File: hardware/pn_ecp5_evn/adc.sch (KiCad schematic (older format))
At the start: 33 parts, among them U801 THS4551, U802 LT6657BHMS8-2.5

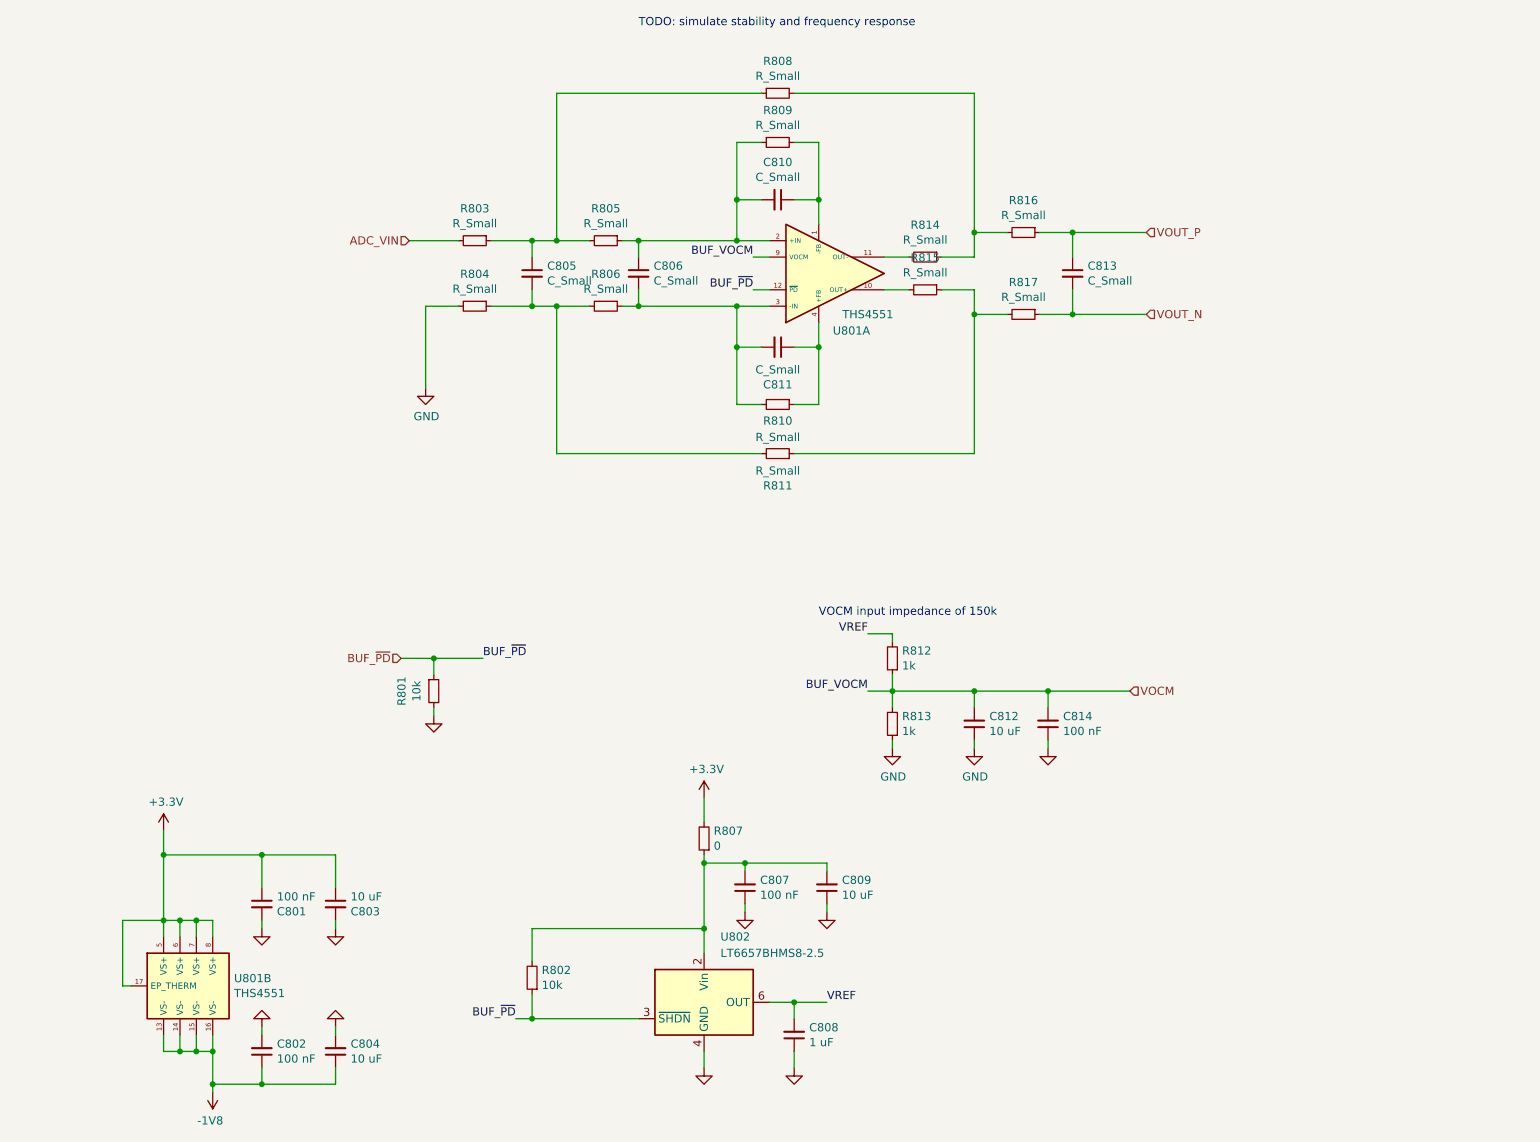
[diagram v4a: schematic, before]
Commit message: checked stability of LO amplifier, started migen project, added more flexibility for active filtering on baseband path
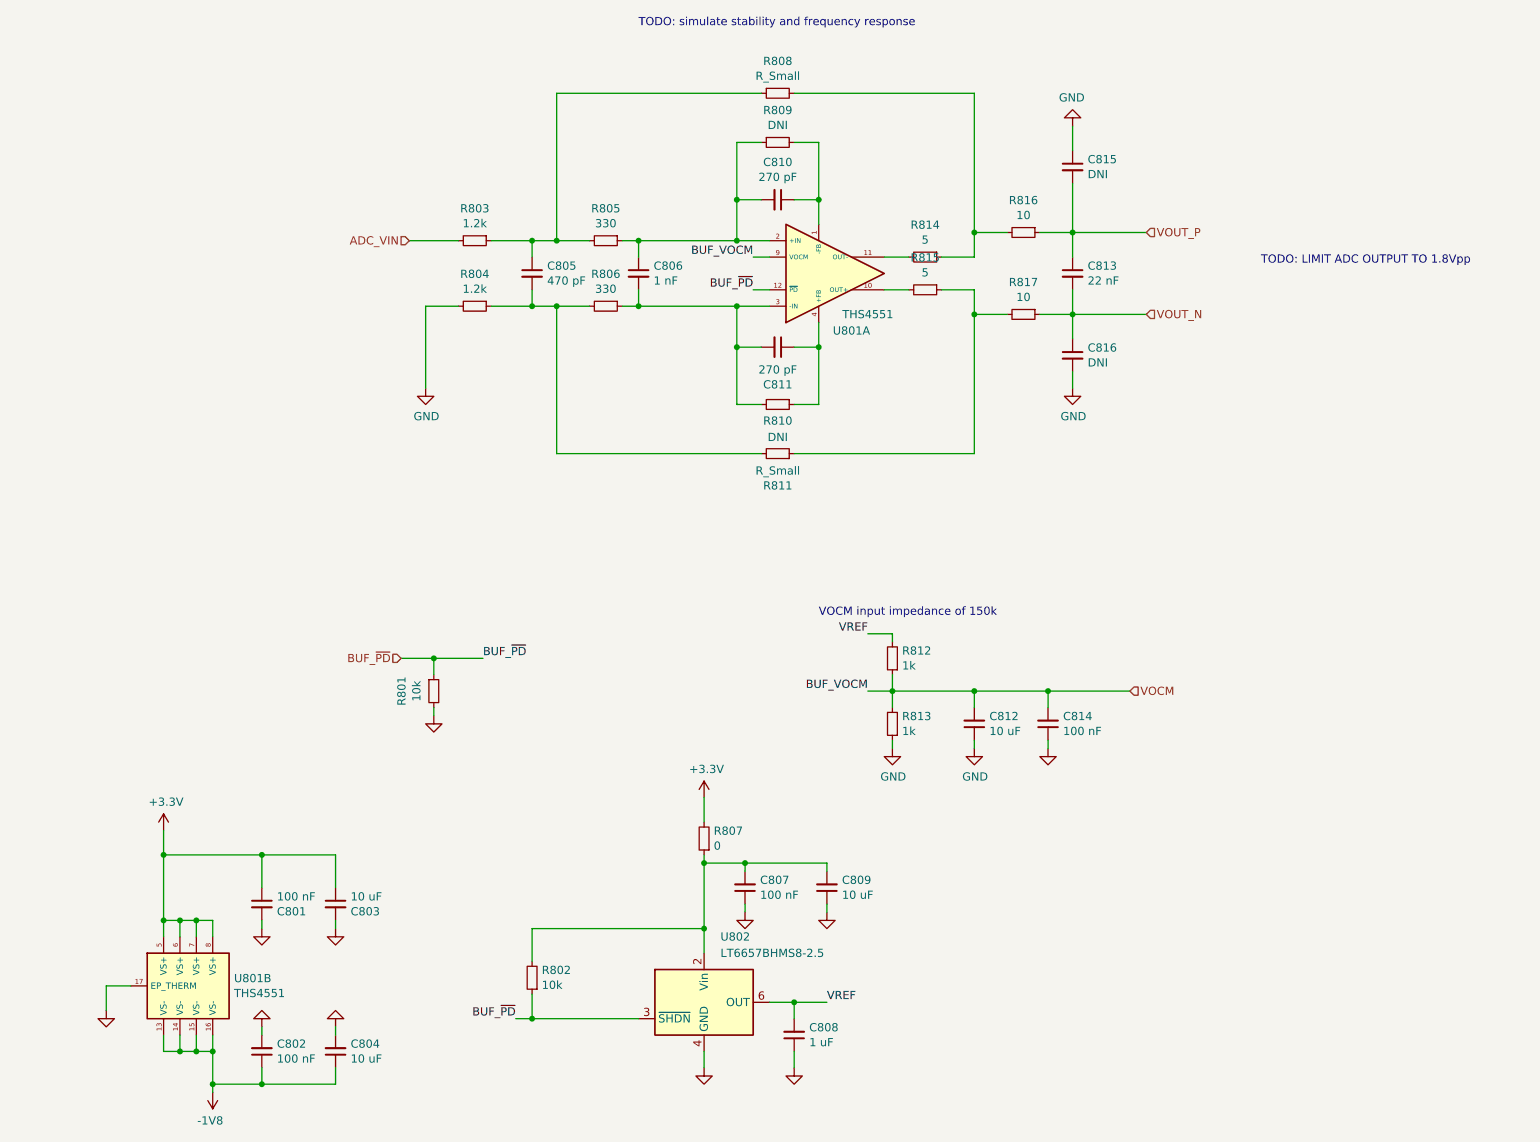
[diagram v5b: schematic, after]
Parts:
- added C815, C816: DNI, Capacitor_SMD:C_0402_1005Metric, symbol Device:C_Small
- C805: value C_Small -> 470 pF; footprint Capacitor_SMD:C_0402_1005Metric -> Capacitor_SMD:C_0603_1608Metric
- C806: value C_Small -> 1 nF
- C810, C811: value C_Small -> 270 pF; footprint Capacitor_SMD:C_0402_1005Metric -> Capacitor_SMD:C_0603_1608Metric
- C813: value C_Small -> 22 nF
- R803, R804: value R_Small -> 1.2k
- R805, R806: value R_Small -> 330
- R809, R810: value R_Small -> DNI
- R814, R815: value R_Small -> 5
- R816, R817: value R_Small -> 10
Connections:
- net +3V3: no longer U801.17 (EP_THERM)
- net GND: now also U801.17 (EP_THERM), C815.1, C816.2
- net VOUT_N: now also C816.1
- net VOUT_P: now also C815.2
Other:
- note added: "TODO: LIMIT ADC OUTPUT TO 1.8Vpp"
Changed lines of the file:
@@
 	2450 6250 2450 6200
-Wire Wire Line
-	1200 6600 1150 6600
-Wire Wire Line
-	1150 6600 1150 6200
-Wire Wire Line
-	1150 6200 1400 6200
 Wire Wire Line
 	2000 5800 2000 6000
@@
 P 6050 2150
 F 0 "R814" V 5854 2150 50  0000 C CNN
-F 1 "R_Small" V 5945 2150 50  0000 C CNN
+F 1 "5" V 5945 2150 50  0000 C CNN
 F 2 "Resistor_SMD:R_0402_1005Metric" H 6050 2150 50  0001 C CNN
 F 3 "~" H 6050 2150 50  0001 C CNN
@@
 P 6050 2350
 F 0 "R815" V 5854 2350 50  0000 C CNN
-F 1 "R_Small" V 5945 2350 50  0000 C CNN
+F 1 "5" V 5945 2350 50  0000 C CNN
 F 2 "Resistor_SMD:R_0402_1005Metric" H 6050 2350 50  0001 C CNN
 F 3 "~" H 6050 2350 50  0001 C CNN
@@
 P 4100 2050
 F 0 "R805" V 3904 2050 50  0000 C CNN
-F 1 "R_Small" V 3995 2050 50  0000 C CNN
+F 1 "330" V 3995 2050 50  0000 C CNN
 F 2 "Resistor_SMD:R_0402_1005Metric" H 4100 2050 50  0001 C CNN
 F 3 "~" H 4100 2050 50  0001 C CNN
@@
 P 4300 2250
 F 0 "C806" H 4392 2296 50  0000 L CNN
-F 1 "C_Small" H 4392 2205 50  0000 L CNN
+F 1 "1 nF" H 4392 2205 50  0000 L CNN
 F 2 "Capacitor_SMD:C_0402_1005Metric" H 4300 2250 50  0001 C CNN
 F 3 "~" H 4300 2250 50  0001 C CNN
@@
 P 5150 2700
 F 0 "C811" V 4921 2700 50  0000 C CNN
-F 1 "C_Small" V 5012 2700 50  0000 C CNN
-F 2 "Capacitor_SMD:C_0402_1005Metric" H 5150 2700 50  0001 C CNN
+F 1 "270 pF" V 5012 2700 50  0000 C CNN
+F 2 "Capacitor_SMD:C_0603_1608Metric" H 5150 2700 50  0001 C CNN
 F 3 "~" H 5150 2700 50  0001 C CNN
 	1    5150 2700
@@
 P 4100 2450
 F 0 "R806" V 3904 2450 50  0000 C CNN
-F 1 "R_Small" V 3995 2450 50  0000 C CNN
+F 1 "330" V 3995 2450 50  0000 C CNN
 F 2 "Resistor_SMD:R_0402_1005Metric" H 4100 2450 50  0001 C CNN
 F 3 "~" H 4100 2450 50  0001 C CNN
@@
 P 3650 2250
 F 0 "C805" H 3742 2296 50  0000 L CNN
-F 1 "C_Small" H 3742 2205 50  0000 L CNN
-F 2 "Capacitor_SMD:C_0402_1005Metric" H 3650 2250 50  0001 C CNN
+F 1 "470 pF" H 3742 2205 50  0000 L CNN
+F 2 "Capacitor_SMD:C_0603_1608Metric" H 3650 2250 50  0001 C CNN
 F 3 "~" H 3650 2250 50  0001 C CNN
 	1    3650 2250
@@
 P 5150 1800
 F 0 "C810" V 4921 1800 50  0000 C CNN
-F 1 "C_Small" V 5012 1800 50  0000 C CNN
-F 2 "Capacitor_SMD:C_0402_1005Metric" H 5150 1800 50  0001 C CNN
+F 1 "270 pF" V 5012 1800 50  0000 C CNN
+F 2 "Capacitor_SMD:C_0603_1608Metric" H 5150 1800 50  0001 C CNN
 F 3 "~" H 5150 1800 50  0001 C CNN
 	1    5150 1800
@@
 P 3300 2450
 F 0 "R804" V 3104 2450 50  0000 C CNN
-F 1 "R_Small" V 3195 2450 50  0000 C CNN
+F 1 "1.2k" V 3195 2450 50  0000 C CNN
 F 2 "Resistor_SMD:R_0402_1005Metric" H 3300 2450 50  0001 C CNN
 F 3 "~" H 3300 2450 50  0001 C CNN
@@
 P 3300 2050
 F 0 "R803" V 3104 2050 50  0000 C CNN
-F 1 "R_Small" V 3195 2050 50  0000 C CNN
+F 1 "1.2k" V 3195 2050 50  0000 C CNN
 F 2 "Resistor_SMD:R_0402_1005Metric" H 3300 2050 50  0001 C CNN
 F 3 "~" H 3300 2050 50  0001 C CNN
@@
 P 6650 2000
 F 0 "R816" V 6454 2000 50  0000 C CNN
-F 1 "R_Small" V 6545 2000 50  0000 C CNN
+F 1 "10" V 6545 2000 50  0000 C CNN
 F 2 "Resistor_SMD:R_0402_1005Metric" H 6650 2000 50  0001 C CNN
 F 3 "~" H 6650 2000 50  0001 C CNN
@@
 P 6650 2500
 F 0 "R817" V 6454 2500 50  0000 C CNN
-F 1 "R_Small" V 6545 2500 50  0000 C CNN
+F 1 "10" V 6545 2500 50  0000 C CNN
 F 2 "Resistor_SMD:R_0402_1005Metric" H 6650 2500 50  0001 C CNN
 F 3 "~" H 6650 2500 50  0001 C CNN
@@
 P 6950 2250
 F 0 "C813" H 6858 2296 50  0000 R CNN
-F 1 "C_Small" H 6858 2205 50  0000 R CNN
+F 1 "22 nF" H 6858 2205 50  0000 R CNN
 F 2 "Capacitor_SMD:C_0402_1005Metric" H 6950 2250 50  0001 C CNN
 F 3 "~" H 6950 2250 50  0001 C CNN
@@
 P 5150 1450
 F 0 "R809" V 4954 1450 50  0000 C CNN
-F 1 "R_Small" V 5045 1450 50  0000 C CNN
+F 1 "DNI" V 5045 1450 50  0000 C CNN
 F 2 "Resistor_SMD:R_0402_1005Metric" H 5150 1450 50  0001 C CNN
 F 3 "~" H 5150 1450 50  0001 C CNN
@@
 P 5150 3050
 F 0 "R810" V 5250 3050 50  0000 C CNN
-F 1 "R_Small" V 5350 3050 50  0000 C CNN
+F 1 "DNI" V 5350 3050 50  0000 C CNN
 F 2 "Resistor_SMD:R_0402_1005Metric" H 5150 3050 50  0001 C CNN
 F 3 "~" H 5150 3050 50  0001 C CNN
@@
 Wire Wire Line
 	6800 4800 6350 4800
+$Comp
+L Device:C_Small C816
+U 1 1 5F6F43A5
+P 6950 2750
+F 0 "C816" H 7042 2796 50  0000 L CNN
+F 1 "DNI" H 7042 2705 50  0000 L CNN
+F 2 "Capacitor_SMD:C_0402_1005Metric" H 6950 2750 50  0001 C CNN
+F 3 "~" H 6950 2750 50  0001 C CNN
+	1    6950 2750
+	1    0    0    -1
+$EndComp
+$Comp
+L Device:C_Small C815
+U 1 1 5F6F59C4
+P 6950 1600
+F 0 "C815" H 7042 1646 50  0000 L CNN
+F 1 "DNI" H 7042 1555 50  0000 L CNN
+F 2 "Capacitor_SMD:C_0402_1005Metric" H 6950 1600 50  0001 C CNN
+F 3 "~" H 6950 1600 50  0001 C CNN
+	1    6950 1600
+	1    0    0    -1
+$EndComp
+$Comp
+L power:GND #PWR0309
+U 1 1 5F6F7134
+P 6950 2950
+F 0 "#PWR0309" H 6950 2700 50  0001 C CNN
+F 1 "GND" H 6955 2777 50  0000 C CNN
+F 2 "" H 6950 2950 50  0001 C CNN
+F 3 "" H 6950 2950 50  0001 C CNN
+	1    6950 2950
+	1    0    0    -1
+$EndComp
+Wire Wire Line
+	6950 2850 6950 2950
+Wire Wire Line
+	6950 2650 6950 2500
+Wire Wire Line
+	6950 2000 6950 1700
+$Comp
+L power:GND #PWR0310
+U 1 1 5F704C70
+P 6950 1350
+F 0 "#PWR0310" H 6950 1100 50  0001 C CNN
+F 1 "GND" H 6955 1177 50  0000 C CNN
+F 2 "" H 6950 1350 50  0001 C CNN
+F 3 "" H 6950 1350 50  0001 C CNN
+	1    6950 1350
+	-1   0    0    1
+$EndComp
+Wire Wire Line
+	6950 1350 6950 1500
+Text Notes 8100 2200 0    50   ~ 0
+TODO: LIMIT ADC OUTPUT TO 1.8Vpp
+$Comp
+L power:GND #PWR0311
+U 1 1 5F76C716
+P 1050 6750
+F 0 "#PWR0311" H 1050 6500 50  0001 C CNN
+F 1 "GND" H 1055 6577 50  0001 C CNN
+F 2 "" H 1050 6750 50  0001 C CNN
+F 3 "" H 1050 6750 50  0001 C CNN
+	1    1050 6750
+	1    0    0    -1
+$EndComp
+Wire Wire Line
+	1050 6600 1050 6750
+Wire Wire Line
+	1050 6600 1200 6600
 $EndSCHEMATC

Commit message: added part numbers to schematic of phase noise downconverter, ordered
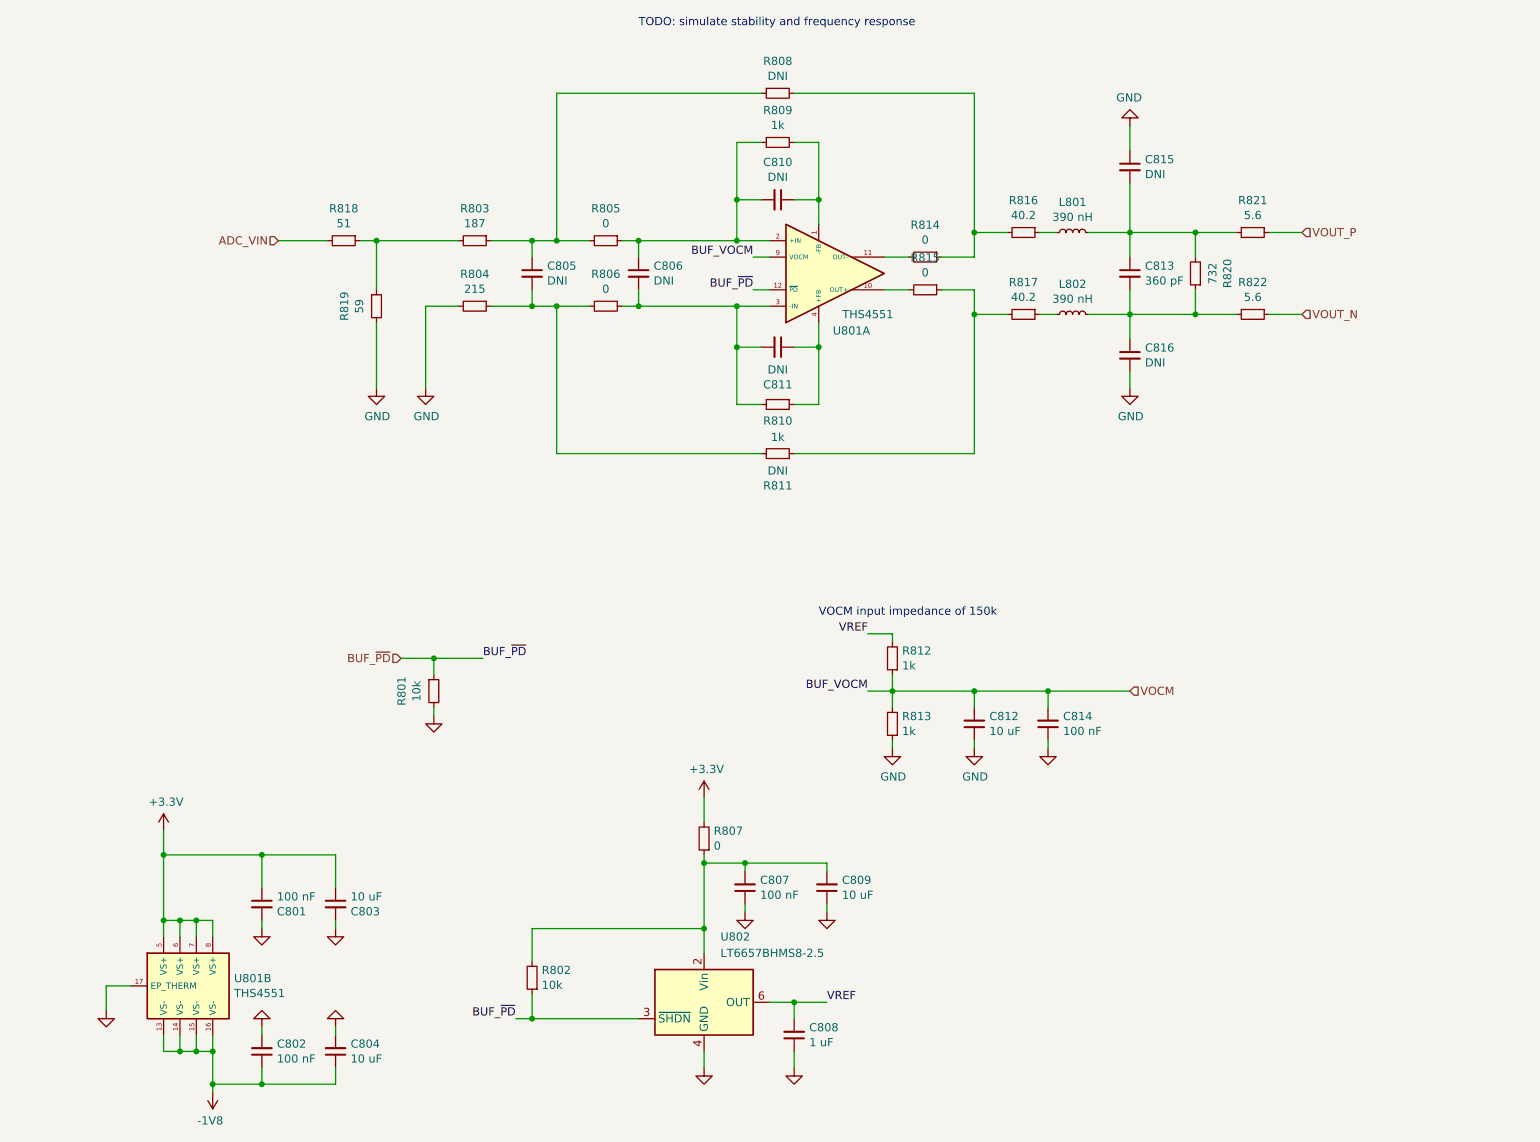
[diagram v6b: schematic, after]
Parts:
- added L801, L802: 390 nH, Inductor_SMD:L_0603_1608Metric, symbol Device:L_Small
- added R818: 51, Resistor_SMD:R_0402_1005Metric, symbol Device:R_Small
- added R819: 59, Resistor_SMD:R_0402_1005Metric, symbol Device:R_Small
- added R820: 732, Resistor_SMD:R_0402_1005Metric, symbol Device:R_Small
- added R821, R822: 5.6, Resistor_SMD:R_0402_1005Metric, symbol Device:R_Small
- C801, C802, C803, C804, C807, C808, C809, C812, C814, C815, C816, R801, R802: Distributor Part Number (none) -> N/A
- C805: value 470 pF -> DNI; Distributor Part Number (none) -> N/A
- C806: value 1 nF -> DNI; Distributor Part Number (none) -> N/A
- C810, C811: value 270 pF -> DNI; Distributor Part Number (none) -> N/A
- C813: value 22 nF -> 360 pF; Distributor Part Number (none) -> N/A
- R803: value 1.2k -> 187; Distributor Part Number (none) -> N/A
- R804: value 1.2k -> 215; Distributor Part Number (none) -> N/A
- R805, R806: value 330 -> 0; Distributor (none) -> Digi-Key; Distributor Part Number (none) -> P0.0JCT-ND
- R807: Distributor (none) -> Digi-Key; Distributor Part Number (none) -> P0.0JCT-ND
- R808, R811: value R_Small -> DNI; Distributor Part Number (none) -> N/A
- R809, R810: value DNI -> 1k; Distributor (none) -> Digi-Key; Distributor Part Number (none) -> RR05P1.0KDCT-ND
- R812, R813: Distributor (none) -> Digi-Key; Distributor Part Number (none) -> RR05P1.0KDCT-ND
- R814, R815: value 5 -> 0; Distributor (none) -> Digi-Key; Distributor Part Number (none) -> P0.0JCT-ND
- R816, R817: value 10 -> 40.2; Distributor Part Number (none) -> N/A
- U801: Distributor (none) -> Digi-Key; Distributor Part Number (none) -> 296-48682-1-ND
- U802: Distributor (none) -> Digi-Key; Distributor Part Number (none) -> LT6657BHMS8-2.5#PBF-ND
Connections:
- net ADC_VIN: now also R818.2; no longer R803.2
- net GND: now also R819.2
- net VOUT_N: now also R822.1; no longer C813.2, C816.1, R817.1
- net VOUT_P: now also R821.1; no longer C813.1, C815.2, R816.1
- new net: R803.2, R818.1, R819.1
- new net: L801.1, R816.1
- new net: C813.1, C815.2, L801.2, R820.2, R821.2
- new net: L802.1, R817.1
- new net: C813.2, C816.1, L802.2, R820.1, R822.2
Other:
- note removed: "TODO: LIMIT ADC OUTPUT TO 1.8Vpp"
- moved on the sheet: C813, C815, C816

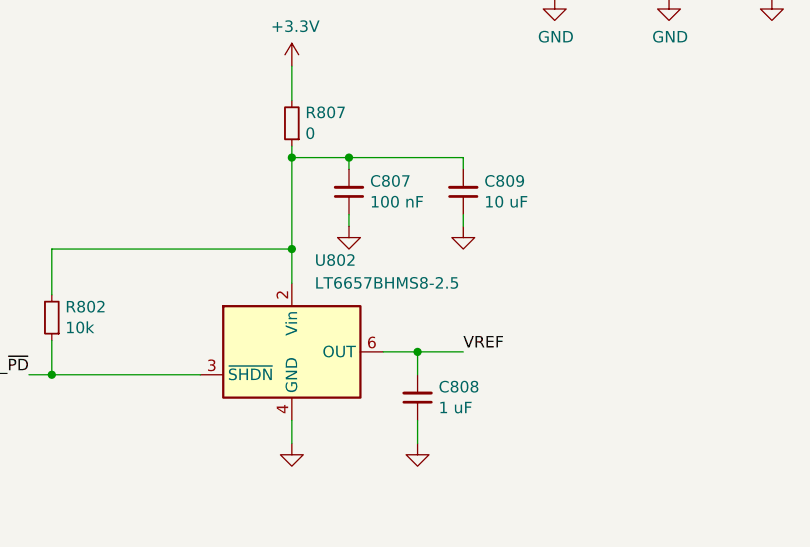
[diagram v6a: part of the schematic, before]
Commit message: added assembly drawing
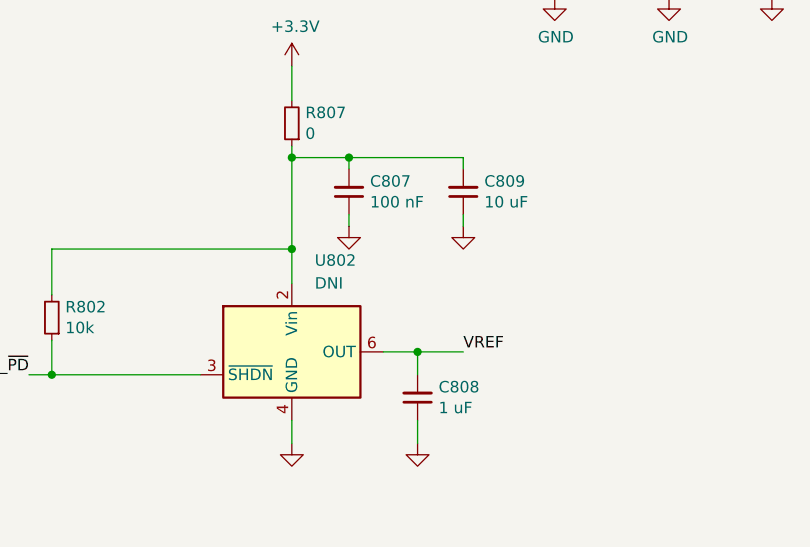
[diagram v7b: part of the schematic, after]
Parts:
- U802: value LT6657BHMS8-2.5 -> DNI
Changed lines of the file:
@@
 P 4700 6700
 F 0 "U802" H 4800 7100 50  0000 L CNN
-F 1 "LT6657BHMS8-2.5" H 4800 7000 50  0000 L CNN
+F 1 "DNI" H 4800 7000 50  0000 L CNN
 F 2 "Package_SO:MSOP-8_3x3mm_P0.65mm" H 4800 7050 50  0001 L CIN
 F 3 "https://www.analog.com/media/en/technical-documentation/data-sheets/6657fd.pdf" H 4750 6350 50  0001 C CIN
